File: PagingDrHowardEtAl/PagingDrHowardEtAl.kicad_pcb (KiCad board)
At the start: 8 copper layers, 179 x 47 mm, 4 parts

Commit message: Complete PagingDrHowardEtAl
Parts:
- added P1: Pulse Playground, PIN_ARRAY_3X1, F.Cu at (162.6, 86.4)
- added P2: 7 segment backpack, PIN_ARRAY_5x1, F.Cu at (160.0, 68.6)
- added P3: Bargraph Backpack, PIN_ARRAY_4x1, F.Cu at (146.1, 68.6)
- added U1: ITSYBITSY, ItsyBitsy, F.Cu at (186.7, 76.2)
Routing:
- net (no net): track 2486.7 -> 1689.1 mm, vias 1236 -> 900
- net /-: track 0.00 -> 250.6 mm, vias 0 -> 84
- net /IO: track 0.00 -> 232.8 mm, vias 0 -> 80
- net /D: track 0.00 -> 200.2 mm, vias 0 -> 77
- net /C: track 0.00 -> 188.0 mm, vias 0 -> 75
- net /+: track 0.00 -> 69.6 mm, vias 0 -> 10
- net /Pulse: track 0.00 -> 39.2 mm, vias 0 -> 10

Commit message: Update PagingDrHowardEtAl.
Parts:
- removed ? (x4): , MH
- moved P2 55.1 mm to (152.4, 123.2)
- moved P3 55.1 mm to (138.4, 123.2)
- moved U1 55.0 mm to (180.3, 130.8)
- moved P1 52.6 mm to (154.9, 138.4), turned to 0 degrees
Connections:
- U1 pad 18: (no net) -> /-
- U1 pad 20: (no net) -> /IO
- U1 pad 30: /+ -> /-
- U1 pad 32: /IO -> /+
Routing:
- net (no net): track 1689.1 -> 0.00 mm, vias 900 -> 0
- net /IO: track 232.8 -> 92.3 mm, vias 80 -> 0
- net /D: track 200.2 -> 62.2 mm, vias 77 -> 0
- net /-: track 250.6 -> 122.8 mm, vias 84 -> 0
- net /C: track 188.0 -> 66.0 mm, vias 75 -> 0
- net /+: track 69.6 -> 49.8 mm, vias 10 -> 0
- net /Pulse: track 39.2 -> 31.8 mm, vias 10 -> 0
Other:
- board outline removed

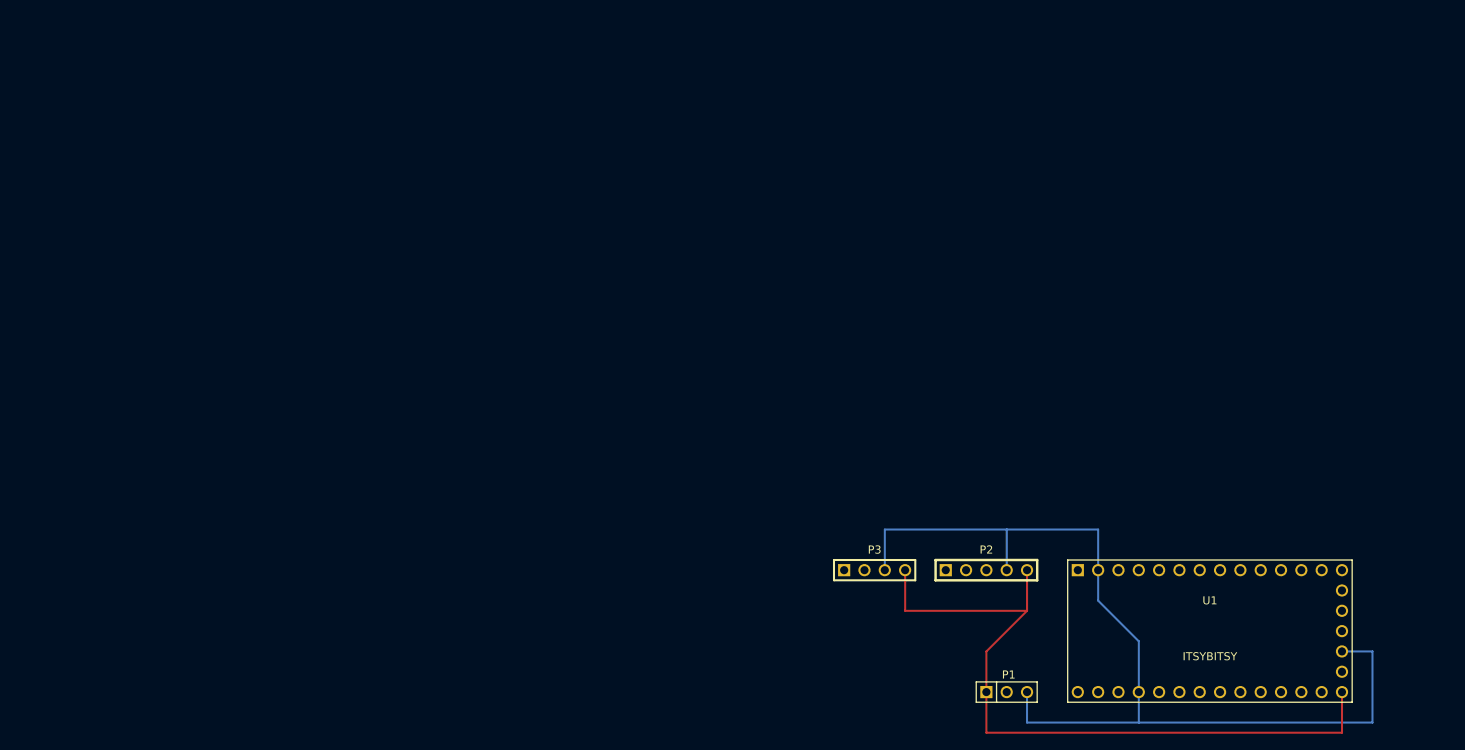
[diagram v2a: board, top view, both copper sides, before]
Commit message: Revert "Update PagingDrHowardEtAl."
This reverts commit db79b4fbad0fb7acf435444e0c859a0f028222a4.
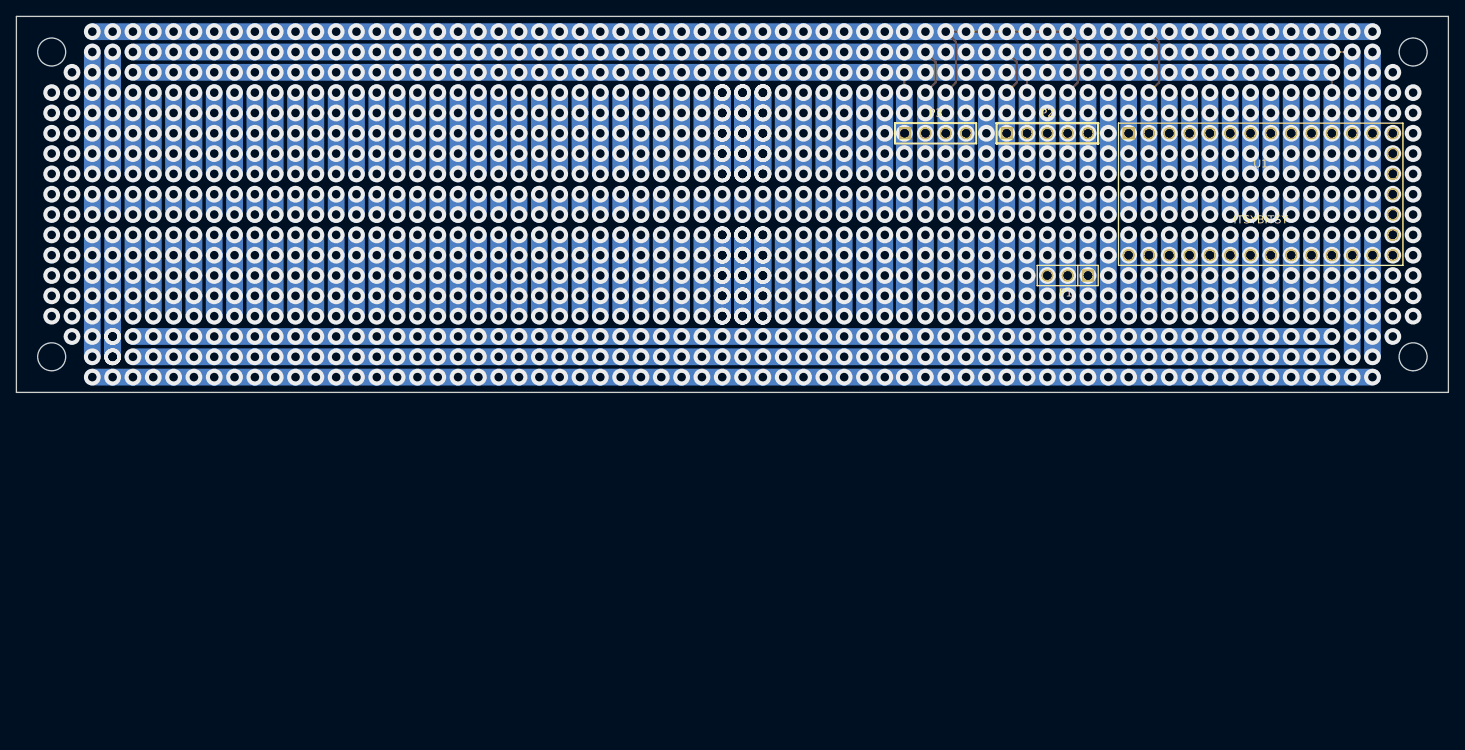
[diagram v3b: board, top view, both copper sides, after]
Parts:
- added ?: , MH, F.Cu at (35.6, 58.4)
- added ?: , MH, F.Cu at (205.7, 58.4)
- added ?: , MH, F.Cu at (205.7, 96.5)
- added ?: , MH, F.Cu at (35.6, 96.5)
- moved P2 55.1 mm to (160.0, 68.6)
- moved P3 55.1 mm to (146.1, 68.6)
- moved U1 55.0 mm to (186.7, 76.2)
- moved P1 52.6 mm to (162.6, 86.4), turned to 180 degrees
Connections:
- U1 pad 18: /- -> (no net)
- U1 pad 20: /IO -> (no net)
- U1 pad 30: /- -> /+
- U1 pad 32: /+ -> /IO
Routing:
- net (no net): track 0.00 -> 1689.1 mm, vias 0 -> 900
- net /IO: track 92.3 -> 232.8 mm, vias 0 -> 80
- net /D: track 62.2 -> 200.2 mm, vias 0 -> 77
- net /-: track 122.8 -> 250.6 mm, vias 0 -> 84
- net /C: track 66.0 -> 188.0 mm, vias 0 -> 75
- net /+: track 49.8 -> 69.6 mm, vias 0 -> 10
- net /Pulse: track 31.8 -> 39.2 mm, vias 0 -> 10
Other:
- board outline added: 179 x 47 mm

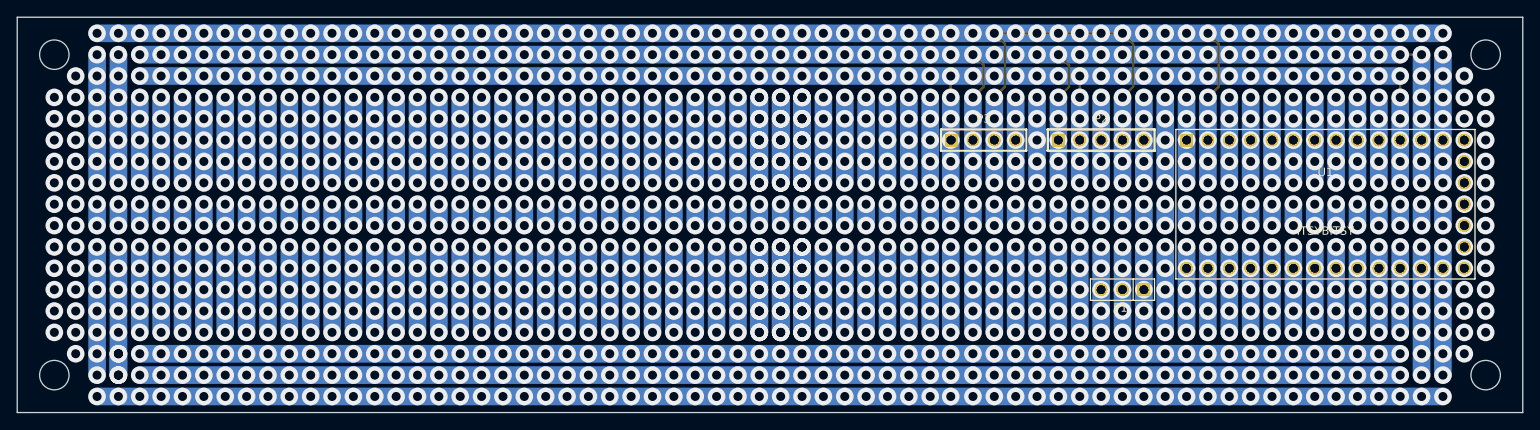
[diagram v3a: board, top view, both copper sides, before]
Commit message: Corrected version of PagingDrHowardEtAl.
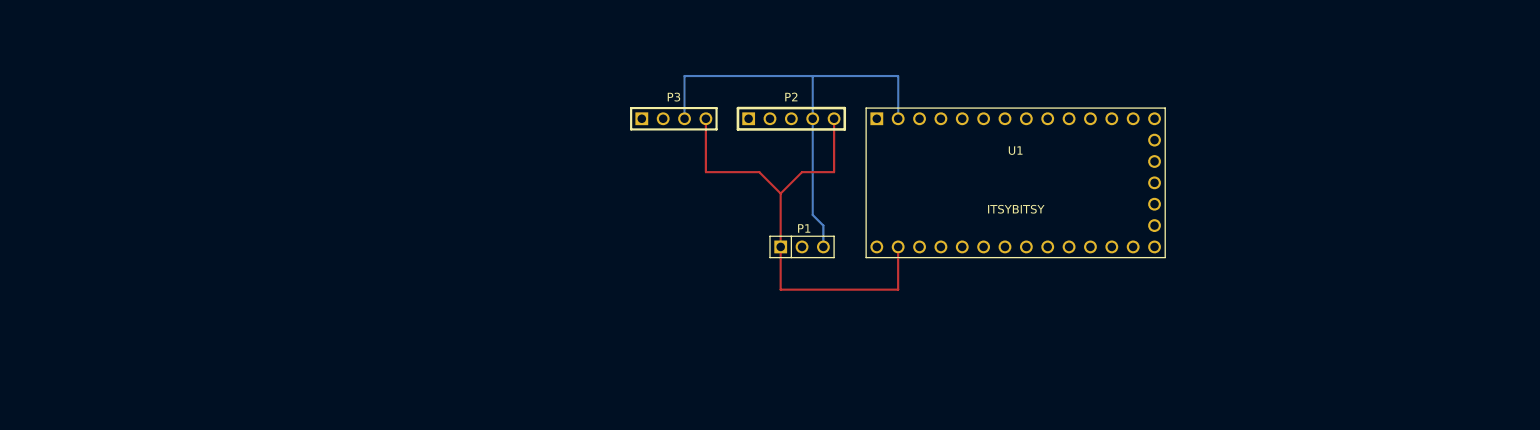
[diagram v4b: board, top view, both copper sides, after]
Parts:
- removed ? (x4): , MH
- moved P1 38.4 mm to (124.5, 81.3), turned to 0 degrees
- moved P2 36.9 mm to (123.2, 66.0)
- moved P3 36.9 mm to (109.2, 66.0)
- moved U1 36.9 mm to (149.9, 73.7)
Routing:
- net (no net): track 1689.1 -> 0.00 mm, vias 900 -> 0
- net /-: track 250.6 -> 56.4 mm, vias 84 -> 0
- net /IO: track 232.8 -> 60.5 mm, vias 80 -> 0
- net /D: track 200.2 -> 64.8 mm, vias 77 -> 0
- net /C: track 188.0 -> 61.0 mm, vias 75 -> 0
- net /+: track 69.6 -> 51.9 mm, vias 10 -> 0
- net /Pulse: track 39.2 -> 26.7 mm, vias 10 -> 0
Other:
- board outline removed

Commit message: Corrected version of PagingDrHowardEtA.
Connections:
- P1 pad 3: /- -> /G
- P2 pad 1: /D -> /SCL
- P2 pad 2: /C -> /SDA
- P2 pad 3: /+ -> /G
- P2 pad 4: /- -> /+5V
- P3 pad 1: /C -> /SCL
- P3 pad 2: /D -> /SDA
- P3 pad 3: /- -> /G
- U1 pad 11: /C -> /SCL
- U1 pad 12: /D -> /SDA
- U1 pad 2: /- -> /G
- U1 pad 30: /+ -> /+5V
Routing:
- net /SDA: track 0.00 -> 64.8 mm
- net /D: track 64.8 -> 0.00 mm
- net /SCL: track 0.00 -> 61.0 mm
- net /C: track 61.0 -> 0.00 mm
- net /G: track 0.00 -> 57.5 mm
- net /-: track 56.4 -> 0.00 mm
- net /+5V: track 0.00 -> 54.4 mm
- net /+: track 51.9 -> 0.00 mm

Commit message: PagingDrHowardEtAl, using an UNO R3
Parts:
- U1: value ITSYBITSY -> UNO; footprint ItsyBitsy -> UNO
- moved P3 35.8 mm to (143.5, 76.2), turned to 180 degrees
- moved P2 25.2 mm to (142.2, 82.5), turned to 180 degrees
- moved P1 19.8 mm to (139.7, 94.0)
- moved U1 8.13 mm to (143.5, 78.7)
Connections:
- P1 pad 1: /IO -> /Vdd
- P2 pad 5: /IO -> /+5V
- P3 pad 4: /IO -> /+5V
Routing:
- net /IO: track 60.5 -> 0.00 mm
- net /Vdd: track 0.00 -> 53.1 mm
- net /G: track 57.5 -> 25.5 mm
- net /SCL: track 61.0 -> 30.8 mm
- net /SDA: track 64.8 -> 36.9 mm
- net /+5V: track 54.4 -> 29.1 mm
- net /Pulse: track 26.7 -> 19.1 mm
